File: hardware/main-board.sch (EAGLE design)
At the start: 1 part, among them U1 ESP32-D0WDQ6

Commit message: added build folder to .gitignore
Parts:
- added C1, C2: 0.1uF, SparkFun-Capacitors:0.1UF-0603-25V-(+80/-20%)
- added C10: 10nF, SparkFun-Capacitors:10NF-0603-50V-10%
- added C3: 1.0uF, SparkFun-Capacitors:1.0UF-0603-16V-10%
- added C4, C7: 0.1uF, SparkFun-Capacitors:0.1UF-0402-16V-10%
- added C5, C8: 1.0uF, SparkFun-Capacitors:1.0UF-0402-16V-10%
- added C6: 10uF, SparkFun-Capacitors:10UF-0805-10V-10%
- added C9: 100PF, SparkFun-Capacitors:100PF-0402-50V-5%
- added IC1, IC2: SI1147, silabs:SI1147
- added L1: 2.7nH/?%/900mA/70mOhm, SparkFun-Coils:INDUCTOR-0402_TIGHT-2.7NH
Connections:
- new net 3.3V: C1.1, C2.1, C3.1, C4.1, C5.1, C6.1, L1.1, U1.VDD3P3_CPU, U1.VDD3P3_RTC, U1.VDD_SDIO
- new net 3.3V_SENSOR_1: IC1.VDD, U1.GPIO0
- new net 3.3V_SENSOR_2: IC2.VDD, U1.GPIO4
- new net GND: C1.2, C10.2, C2.2, C3.2, C4.2, C5.2, C6.2, C7.2, C8.2, C9.2
- new net N$1: C10.1, U1.CAP1
- new net N$2: C7.1, C8.1, C9.1, U1.VDDA
- new net N$3: L1.2, U1.VDD3P3
- new net PROX_INT_1: IC1.INT
- new net PROX_INT_2: IC2.INT
- new net SCL: IC1.SCL, IC2.SCL, U1.GPIO2
- new net SDA: IC1.SDA, IC2.SDA, U1.MTDO
- new net SPKR_NEG: U1.GPIO26
- new net SPKR_POS: U1.GPIO25

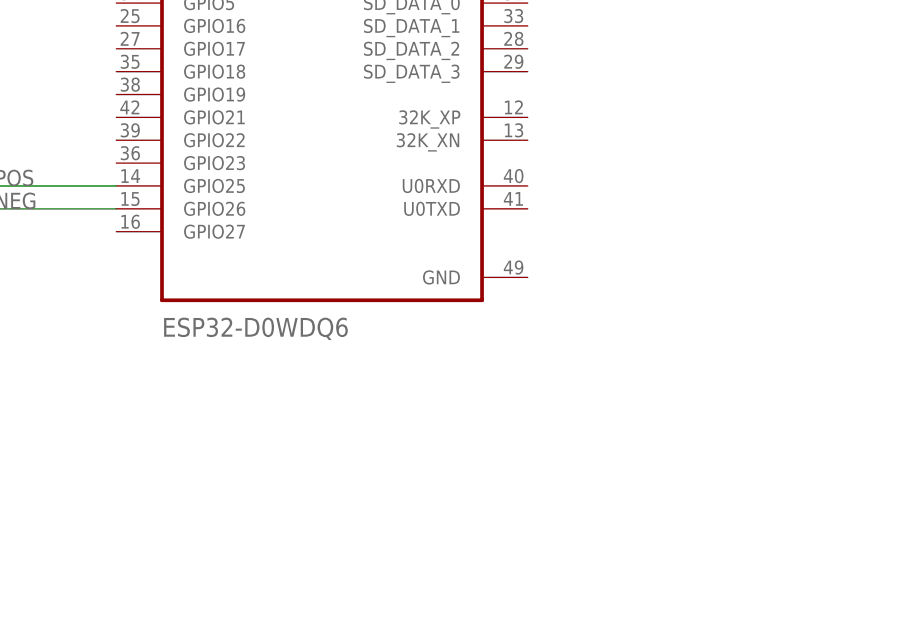
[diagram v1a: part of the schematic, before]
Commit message: added tx/rx pins for programming
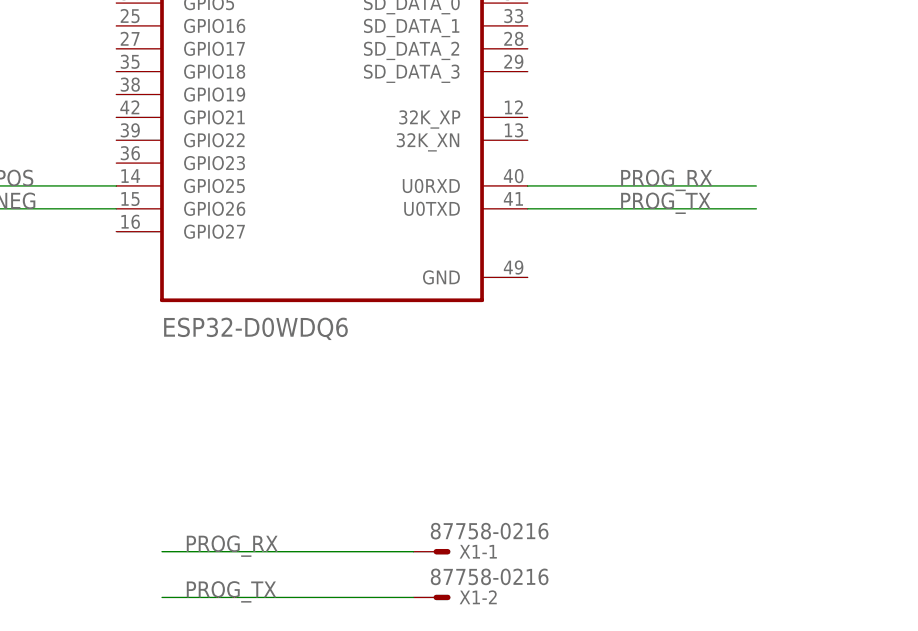
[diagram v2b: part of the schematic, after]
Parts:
- added X1: 87758-0216, con-molex:87758-0216
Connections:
- new net PROG_RX: U1.U0RXD, X1-1.S
- new net PROG_TX: U1.U0TXD, X1-2.S
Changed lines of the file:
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@@
 <part name="L1" library="SparkFun-Coils" deviceset="INDUCTOR" device="-0402_TIGHT-2.7NH" value="2.7nH/?%/900mA/70mOhm"/>
 <part name="C10" library="SparkFun-Capacitors" deviceset="10NF" device="-0603-50V-10%" value="10nF"/>
+<part name="X1" library="con-molex" library_urn="urn:adsk.eagle:library:165" deviceset="87758-0216" device="" package3d_urn="urn:adsk.eagle:package:8078894/1"/>
 </parts>
 <sheets>
@@
 <attribute name="NAME" x="-21.336" y="76.581" size="1.778" layer="95" font="vector"/>
 <attribute name="VALUE" x="-21.336" y="71.501" size="1.778" layer="96" font="vector"/>
+</instance>
+<instance part="X1" gate="-1" x="53.34" y="-15.24" smashed="yes">
+<attribute name="NAME" x="55.88" y="-16.002" size="1.524" layer="95"/>
+<attribute name="VALUE" x="52.578" y="-13.843" size="1.778" layer="96"/>
+</instance>
+<instance part="X1" gate="-2" x="53.34" y="-20.32" smashed="yes">
+<attribute name="NAME" x="55.88" y="-21.082" size="1.524" layer="95"/>
+<attribute name="VALUE" x="52.578" y="-18.923" size="1.778" layer="96"/>
 </instance>
 </instances>
@@
 </segment>
 </net>
+<net name="PROG_RX" class="0">
+<segment>
+<pinref part="U1" gate="G$1" pin="U0RXD"/>
+<wire x1="63.5" y1="25.4" x2="88.9" y2="25.4" width="0.1524" layer="91"/>
+<label x="73.66" y="25.4" size="1.778" layer="95"/>
+</segment>
+<segment>
+<pinref part="X1" gate="-1" pin="S"/>
+<wire x1="50.8" y1="-15.24" x2="22.86" y2="-15.24" width="0.1524" layer="91"/>
+<label x="25.4" y="-15.24" size="1.778" layer="95"/>
+</segment>
+</net>
+<net name="PROG_TX" class="0">
+<segment>
+<pinref part="U1" gate="G$1" pin="U0TXD"/>
+<wire x1="88.9" y1="22.86" x2="63.5" y2="22.86" width="0.1524" layer="91"/>
+<label x="73.66" y="22.86" size="1.778" layer="95"/>
+</segment>
+<segment>
+<pinref part="X1" gate="-2" pin="S"/>
+<wire x1="22.86" y1="-20.32" x2="50.8" y2="-20.32" width="0.1524" layer="91"/>
+<label x="25.4" y="-20.32" size="1.778" layer="95"/>
+</segment>
+</net>
